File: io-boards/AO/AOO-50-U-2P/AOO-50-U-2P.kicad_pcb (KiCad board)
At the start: 2 copper layers, 50 x 33 mm, 20 parts, among them J1 GPP_Conn_01x12_Pin, J2 Conn_01x02_Socket, J3 Conn_01x02_Socket, U1 PC817, U3 LM358

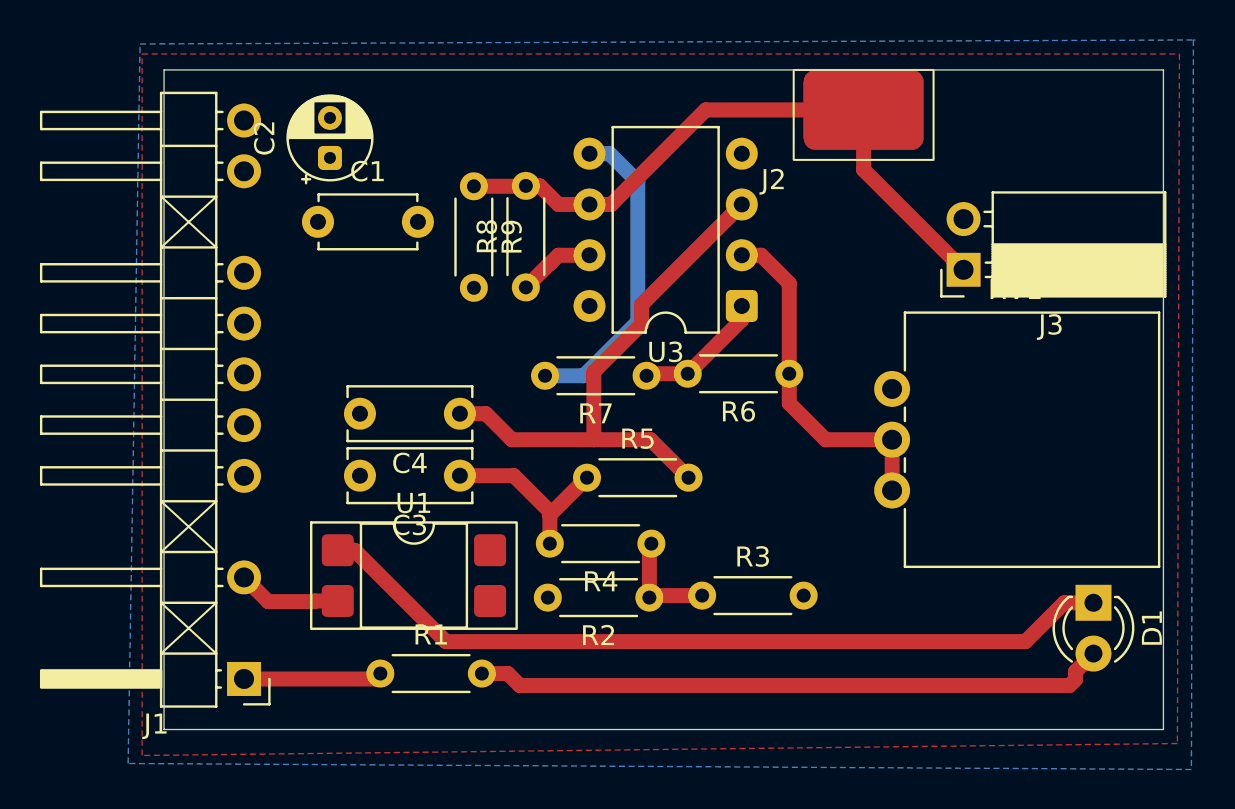
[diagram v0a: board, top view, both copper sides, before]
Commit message: Made some corrections after assembling of prototype PCBs
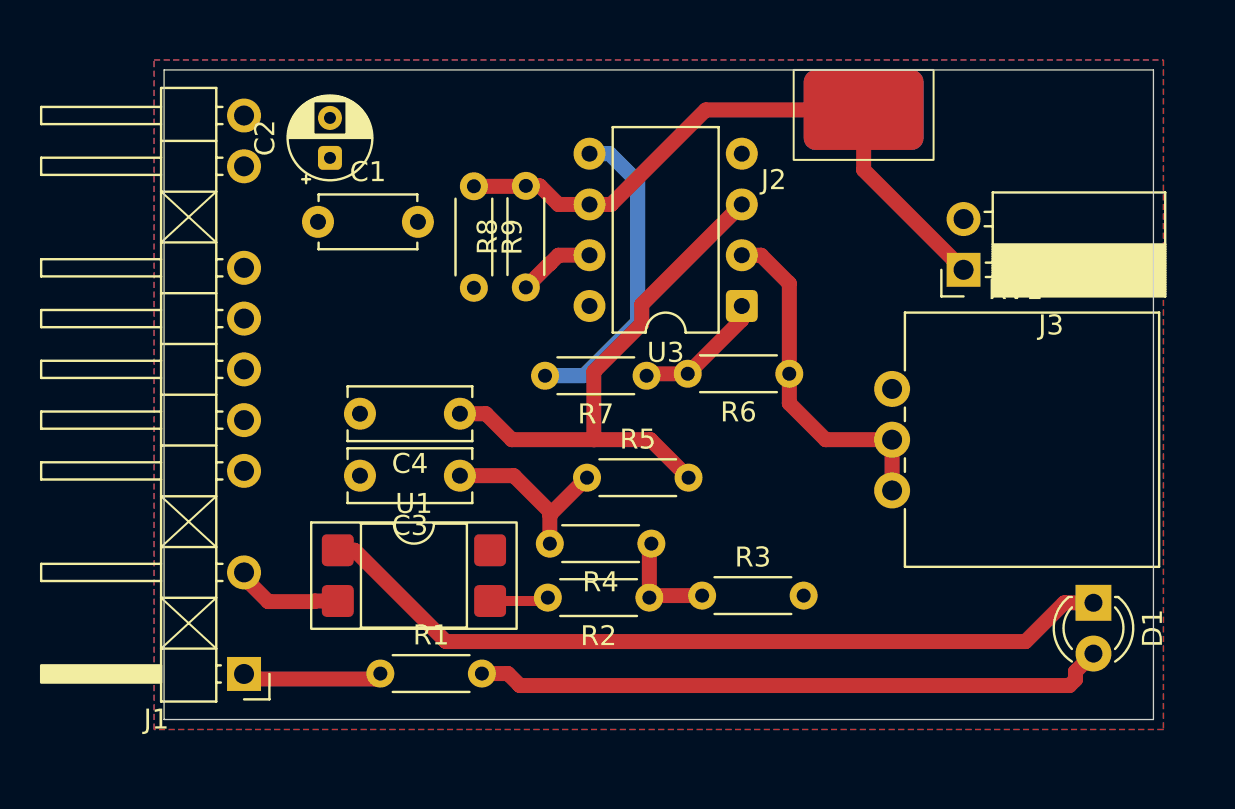
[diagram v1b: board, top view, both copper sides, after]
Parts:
- moved J1 0.25 mm to (104.0, 80.2)
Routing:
- net Net-(R2-Pad2): track 0.00 -> 2.96 mm
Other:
- board size 50 x 33 mm -> 49.5 x 32.5 mm
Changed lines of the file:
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@@
 	(footprint "tuxmio:IO_GPP_PinHeader_1x12_P2.54mm_Horizontal"
 		(layer "F.Cu")
-		(at 104 80.47 180)
+		(at 104 80.22 180)
 		(descr "Through hole angled pin header, 1x12, 2.54mm pitch, 6mm pin length, single row")
 		(tags "Through hole angled pin header THT 1x12 2.54mm single row")
@@
 	(gr_rect
 		(start 100 50)
-		(end 150 83)
+		(end 149.5 82.5)
 		(stroke
 			(width 0.05)
@@
 	)
 	(segment
-		(start 104 75.39)
-		(end 105.21 76.6)
+		(start 104 75.14)
+		(end 104 75.39)
+		(width 0.75)
+		(layer "F.Cu")
+		(net 7)
+	)
+	(segment
+		(start 105.21 76.6)
+		(end 107.5 76.6)
 		(width 0.75)
 		(layer "F.Cu")
@@
 	)
 	(segment
-		(start 105.21 76.6)
-		(end 107.5 76.6)
+		(start 104 75.39)
+		(end 105.21 76.6)
 		(width 0.75)
 		(layer "F.Cu")
@@
 	)
 	(segment
-		(start 110.55 80.47)
-		(end 110.82 80.2)
+		(start 104.25 80.47)
+		(end 110.55 80.47)
 		(width 0.75)
 		(layer "F.Cu")
@@
 	)
 	(segment
-		(start 104 80.47)
-		(end 110.55 80.47)
+		(start 104 80.22)
+		(end 104.25 80.47)
+		(width 0.75)
+		(layer "F.Cu")
+		(net 10)
+	)
+	(segment
+		(start 110.55 80.47)
+		(end 110.82 80.2)
 		(width 0.75)
 		(layer "F.Cu")
@@
 	)
 	(segment
+		(start 119.03 76.57)
+		(end 119.2 76.4)
+		(width 0.5)
+		(layer "F.Cu")
+		(net 16)
+	)
+	(segment
+		(start 116.31 76.57)
+		(end 119.03 76.57)
+		(width 0.5)
+		(layer "F.Cu")
+		(net 16)
+	)
+	(segment
 		(start 133.1 68.5)
 		(end 136.425 68.5)
@@
 		(polygon
 			(pts
-				(xy 98.9 49.2) (xy 150.8 49.2) (xy 150.7 83.7) (xy 98.9 84.3)
+				(xy 99.5 49.5) (xy 150 49.5) (xy 150 83) (xy 99.5 83)
 			)
 		)
@@
 		(polygon
 			(pts
-				(xy 151.6 48.5) (xy 151.5 48.5) (xy 151.4 85) (xy 98.2 84.7) (xy 98.8 48.7)
+				(xy 150 49.5) (xy 150 83) (xy 99.5 83) (xy 99.5 49.5)
 			)
 		)
